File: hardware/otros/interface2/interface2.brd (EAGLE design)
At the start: 73.6 x 18.7 mm, 8 parts

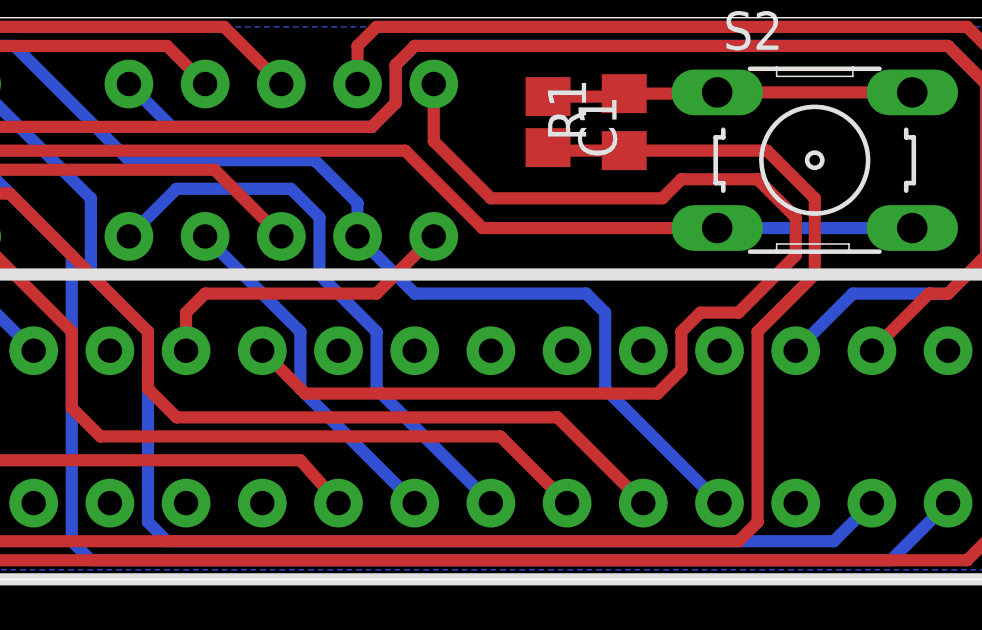
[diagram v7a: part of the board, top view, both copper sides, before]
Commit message: 
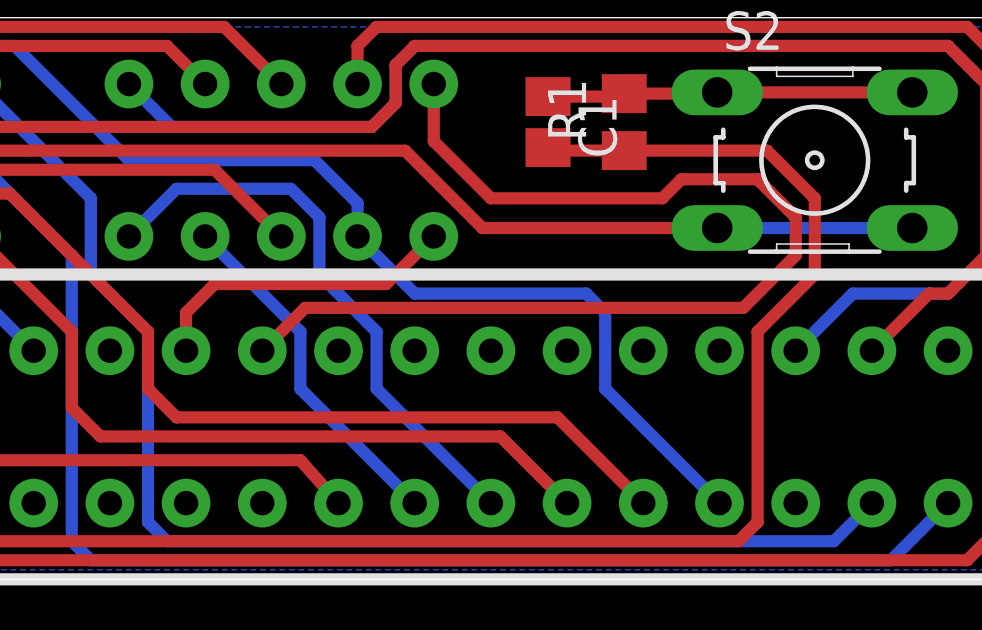
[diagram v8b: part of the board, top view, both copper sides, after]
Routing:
- net WR: track 37.8 -> 35.9 mm
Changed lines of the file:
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@@
 <contactref element="U$3" pad="B18"/>
 <wire x1="45.72" y1="7.62" x2="45.72" y2="8.89" width="0.4064" layer="1"/>
-<wire x1="45.72" y1="8.89" x2="46.355" y2="9.525" width="0.4064" layer="1"/>
-<wire x1="46.355" y1="9.525" x2="52.07" y2="9.525" width="0.4064" layer="1"/>
-<wire x1="52.07" y1="9.525" x2="53.975" y2="11.43" width="0.4064" layer="1"/>
+<wire x1="45.72" y1="8.89" x2="46.6725" y2="9.8425" width="0.4064" layer="1"/>
+<wire x1="46.6725" y1="9.8425" x2="52.3875" y2="9.8425" width="0.4064" layer="1"/>
+<wire x1="52.3875" y1="9.8425" x2="53.975" y2="11.43" width="0.4064" layer="1"/>
 </signal>
 <signal name="WR">
 <contactref element="U$1" pad="WR"/>
 <contactref element="U$3" pad="B19"/>
-<wire x1="48.26" y1="7.62" x2="49.68875" y2="6.19125" width="0.4064" layer="1"/>
-<wire x1="49.68875" y1="6.19125" x2="61.43625" y2="6.19125" width="0.4064" layer="1"/>
-<wire x1="61.43625" y1="6.19125" x2="62.23" y2="6.985" width="0.4064" layer="1"/>
-<wire x1="62.23" y1="6.985" x2="62.23" y2="8.255" width="0.4064" layer="1"/>
-<wire x1="62.23" y1="8.255" x2="62.865" y2="8.89" width="0.4064" layer="1"/>
-<wire x1="62.865" y1="8.89" x2="64.135" y2="8.89" width="0.4064" layer="1"/>
-<wire x1="64.135" y1="8.89" x2="66.04" y2="10.795" width="0.4064" layer="1"/>
+<wire x1="64.29375" y1="9.04875" x2="66.04" y2="10.795" width="0.4064" layer="1"/>
 <wire x1="66.04" y1="10.795" x2="66.04" y2="12.065" width="0.4064" layer="1"/>
 <wire x1="66.04" y1="12.065" x2="64.77" y2="13.335" width="0.4064" layer="1"/>
@@
 <wire x1="55.88" y1="12.7" x2="53.975" y2="14.605" width="0.4064" layer="1"/>
 <wire x1="53.975" y1="14.605" x2="53.975" y2="16.51" width="0.4064" layer="1"/>
+<wire x1="64.29375" y1="9.04875" x2="49.68875" y2="9.04875" width="0.4064" layer="1"/>
+<wire x1="49.68875" y1="9.04875" x2="48.26" y2="7.62" width="0.4064" layer="1"/>
 </signal>
 <signal name="N$1">
